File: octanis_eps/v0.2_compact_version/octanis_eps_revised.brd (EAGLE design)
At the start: 61.9 x 49.5 mm, 96 parts, among them IC1 OPA2333DGK, IC5 OPA2333DGK, IC7 OPA2333DGK, IC9 OPA2333DGK, Q1 FC-12M, Q2 N-HEXFET-2D_SOT232-, Q3 N-HEXFET-2D_SOT232-, Q4 N-HEXFET-2D_SOT232-

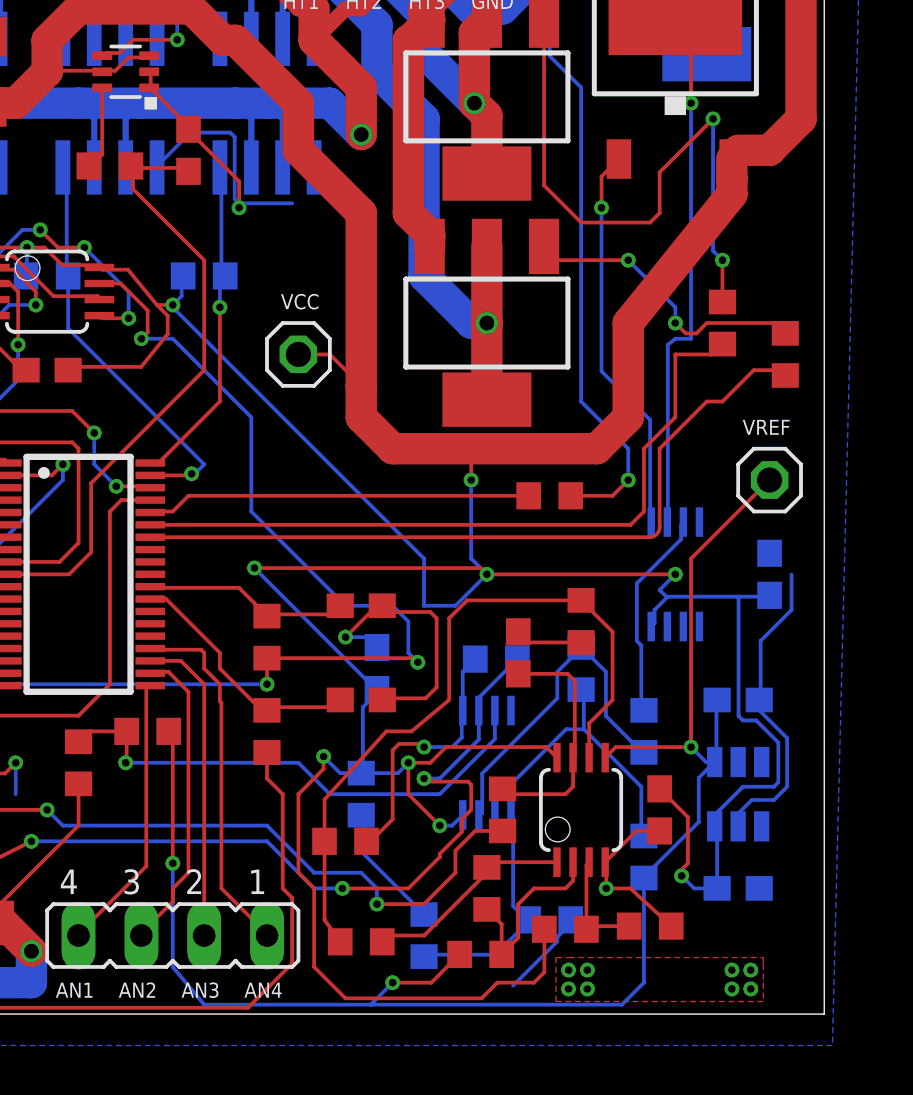
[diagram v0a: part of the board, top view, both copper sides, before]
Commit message: added pull down on heat EN entries
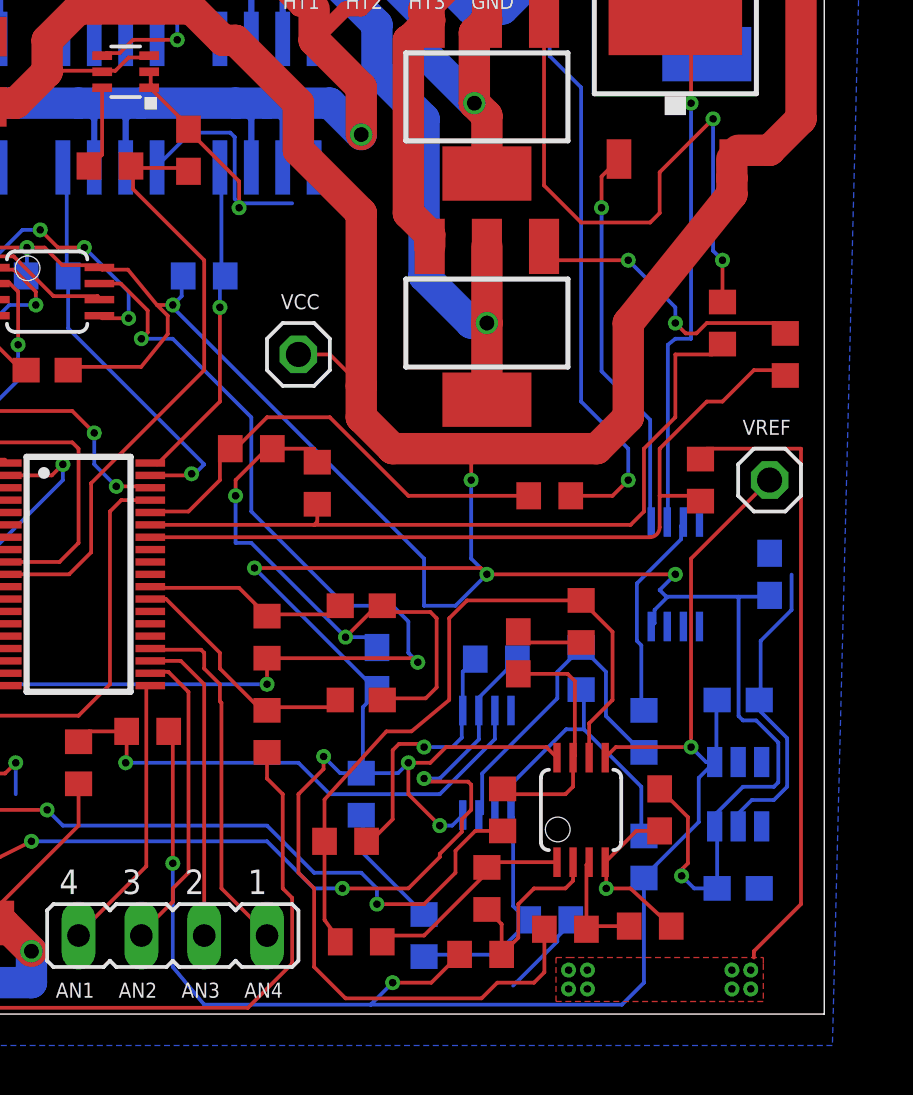
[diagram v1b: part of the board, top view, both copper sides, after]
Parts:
- added R42, R43, R44: 1M, rcl:R0603
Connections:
- net EN_HEAT1: now also R42.1
- net EN_HEAT2: now also R43.1
- net EN_HEAT3: now also R44.1
- net GND: now also R42.2, R43.2, R44.2
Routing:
- net GND: track 243.3 -> 282.0 mm, vias 28 -> 29
- net EN_HEAT3: track 15.6 -> 18.9 mm
- net EN_HEAT1: track 30.4 -> 32.1 mm
- net EN_HEAT2: track 29.1 -> 30.0 mm
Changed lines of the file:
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@@
 <attribute name="VALUE" x="39.37" y="53.975" size="1.27" layer="27"/>
+</element>
+<element name="R42" library="rcl" package="R0603" value="1M" x="56.896" y="52.07" smashed="yes" rot="R90">
+<attribute name="VALUE" x="57.785" y="50.419" size="1.27" layer="27" rot="R180"/>
+</element>
+<element name="R43" library="rcl" package="R0603" value="1M" x="41.402" y="51.943" smashed="yes" rot="R90">
+<attribute name="VALUE" x="43.307" y="50.8" size="1.27" layer="27" rot="R90"/>
+</element>
+<element name="R44" library="rcl" package="R0603" value="1M" x="38.735" y="53.34" smashed="yes">
+<attribute name="VALUE" x="37.592" y="53.975" size="1.27" layer="27"/>
 </element>
 </elements>
@@
 <wire x1="19.685" y1="53.34" x2="19.05" y2="53.34" width="0.1524" layer="16"/>
 <wire x1="19.05" y1="53.34" x2="18.8611" y2="53.5289" width="0.1524" layer="16"/>
+<contactref element="R43" pad="2"/>
+<contactref element="R44" pad="2"/>
+<contactref element="R42" pad="2"/>
+<wire x1="41.275" y1="53.34" x2="39.585" y2="53.34" width="0.1524" layer="1"/>
+<wire x1="41.275" y1="52.705" x2="41.275" y2="53.34" width="0.1524" layer="1"/>
+<wire x1="41.275" y1="52.705" x2="41.402" y2="52.793" width="0.1524" layer="1"/>
+<wire x1="60.96" y1="53.34" x2="57.15" y2="53.34" width="0.1524" layer="1"/>
+<wire x1="60.96" y1="34.925" x2="60.96" y2="53.34" width="0.1524" layer="1"/>
+<wire x1="59.055" y1="33.02" x2="60.96" y2="34.925" width="0.1524" layer="1"/>
+<wire x1="57.15" y1="53.34" x2="56.896" y2="52.92" width="0.1524" layer="1"/>
+<wire x1="59.055" y1="33.02" x2="59.055" y2="32.766" width="0.1524" layer="1"/>
+<wire x1="38.1" y1="52.07" x2="39.37" y2="53.34" width="0.1524" layer="1"/>
+<wire x1="38.1" y1="51.435" x2="38.1" y2="52.07" width="0.1524" layer="1"/>
+<wire x1="38.1" y1="49.53" x2="38.1" y2="51.435" width="0.1524" layer="16"/>
+<wire x1="38.735" y1="49.53" x2="38.1" y2="49.53" width="0.1524" layer="16"/>
+<wire x1="42.545" y1="45.72" x2="38.735" y2="49.53" width="0.1524" layer="16"/>
+<wire x1="39.37" y1="53.34" x2="39.585" y2="53.34" width="0.1524" layer="1"/>
+<via x="38.1" y="51.435" extent="1-16" drill="0.3048"/>
 </signal>
 <signal name="VCC">
@@
 <wire x1="35.3545" y1="57.9741" x2="35.3545" y2="58.717" width="0.1524" layer="1"/>
 <wire x1="35.3545" y1="58.717" x2="34.9218" y2="59.1497" width="0.1524" layer="1"/>
-<wire x1="58.42" y1="65.405" x2="58.16" y2="65.05" width="0" layer="19" extent="1-1"/>
+<wire x1="58.42" y1="65.405" x2="58.16" y2="65.05" width="0.1524" layer="1"/>
 </signal>
 <signal name="VREF">
@@
 <wire x1="34.65" y1="49.76" x2="54.84" y2="49.76" width="0.1524" layer="1"/>
 <wire x1="54.84" y1="49.76" x2="55.245" y2="50.165" width="0.1524" layer="1" curve="90"/>
-<wire x1="55.245" y1="50.165" x2="55.245" y2="53.34" width="0.1524" layer="1"/>
+<wire x1="55.245" y1="50.165" x2="55.245" y2="51.435" width="0.1524" layer="1"/>
+<wire x1="55.245" y1="51.435" x2="55.245" y2="53.34" width="0.1524" layer="1"/>
 <wire x1="55.245" y1="53.34" x2="57.15" y2="55.245" width="0.1524" layer="1"/>
 <wire x1="57.15" y1="55.245" x2="57.785" y2="55.245" width="0.1524" layer="1"/>
@@
 <wire x1="59.055" y1="56.515" x2="60.11" y2="56.515" width="0.1524" layer="1"/>
 <wire x1="60.11" y1="56.515" x2="60.325" y2="56.3" width="0.1524" layer="1"/>
+<contactref element="R42" pad="1"/>
+<wire x1="55.245" y1="51.435" x2="56.515" y2="51.435" width="0.1524" layer="1"/>
+<wire x1="56.515" y1="51.435" x2="56.896" y2="51.22" width="0.1524" layer="1"/>
 </signal>
 <signal name="EN_HEAT2">
 <contactref element="R2" pad="2"/>
 <contactref element="U$6" pad="33"/>
-<wire x1="34.65" y1="50.26" x2="54.07" y2="50.26" width="0.1524" layer="1"/>
+<wire x1="34.65" y1="50.26" x2="41.275" y2="50.26" width="0.1524" layer="1"/>
+<wire x1="41.275" y1="50.26" x2="54.07" y2="50.26" width="0.1524" layer="1"/>
 <wire x1="54.07" y1="50.26" x2="54.61" y2="50.8" width="0.1524" layer="1"/>
 <wire x1="54.61" y1="50.8" x2="54.61" y2="53.34" width="0.1524" layer="1"/>
@@
 <wire x1="55.88" y1="57.15" x2="57.365" y2="57.15" width="0.1524" layer="1"/>
 <wire x1="57.365" y1="57.15" x2="57.785" y2="57.57" width="0.1524" layer="1"/>
+<contactref element="R43" pad="1"/>
+<wire x1="41.402" y1="51.093" x2="41.402" y2="50.387" width="0.1524" layer="1"/>
+<wire x1="41.402" y1="50.387" x2="41.275" y2="50.26" width="0.1524" layer="1"/>
 </signal>
 <signal name="N$37">
@@
 <contactref element="R3" pad="2"/>
 <contactref element="U$6" pad="34"/>
-<wire x1="49.95" y1="51.435" x2="36.195" y2="51.435" width="0.1524" layer="1"/>
-<wire x1="36.195" y1="51.435" x2="35.56" y2="50.8" width="0.1524" layer="1"/>
-<wire x1="35.56" y1="50.8" x2="34.69" y2="50.8" width="0.1524" layer="1"/>
-<wire x1="34.69" y1="50.8" x2="34.65" y2="50.76" width="0.1524" layer="1"/>
+<contactref element="R44" pad="1"/>
+<wire x1="41.91" y1="54.61" x2="45.085" y2="51.435" width="0.1524" layer="1"/>
+<wire x1="45.085" y1="51.435" x2="49.95" y2="51.435" width="0.1524" layer="1"/>
+<wire x1="37.465" y1="52.07" x2="37.465" y2="53.34" width="0.1524" layer="1"/>
+<wire x1="36.195" y1="50.8" x2="37.465" y2="52.07" width="0.1524" layer="1"/>
+<wire x1="34.925" y1="50.8" x2="36.195" y2="50.8" width="0.1524" layer="1"/>
+<wire x1="37.465" y1="53.34" x2="37.885" y2="53.34" width="0.1524" layer="1"/>
+<wire x1="34.925" y1="50.8" x2="34.65" y2="50.76" width="0.1524" layer="1"/>
+<wire x1="39.37" y1="54.61" x2="38.1" y2="53.34" width="0.1524" layer="1"/>
+<wire x1="41.91" y1="54.61" x2="39.37" y2="54.61" width="0.1524" layer="1"/>
+<wire x1="38.1" y1="53.34" x2="37.885" y2="53.34" width="0.1524" layer="1"/>
 </signal>
 <signal name="DISSIP">

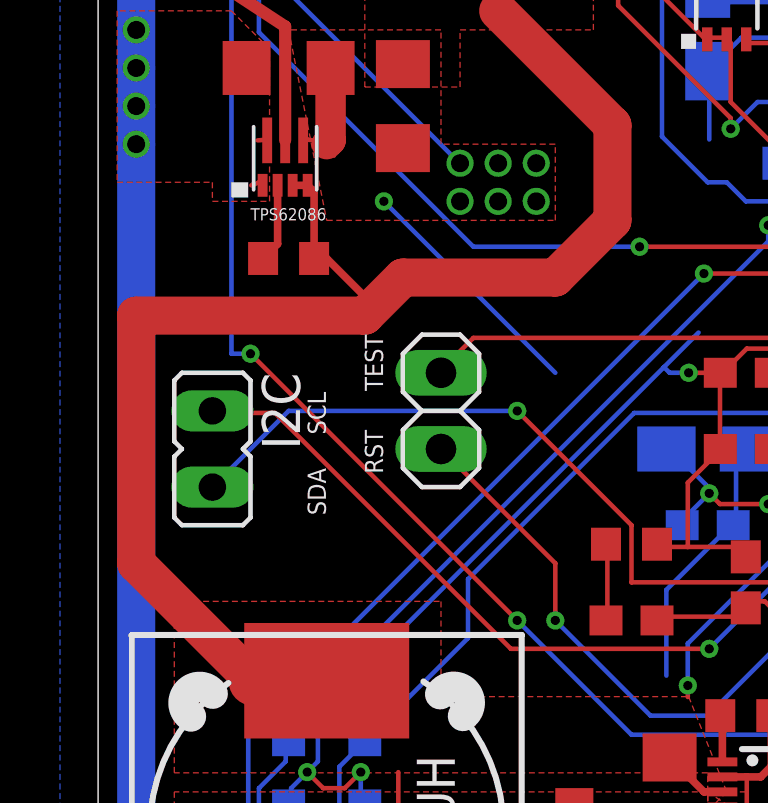
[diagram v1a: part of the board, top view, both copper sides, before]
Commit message: added 0Ohm jumper on discharge circuit
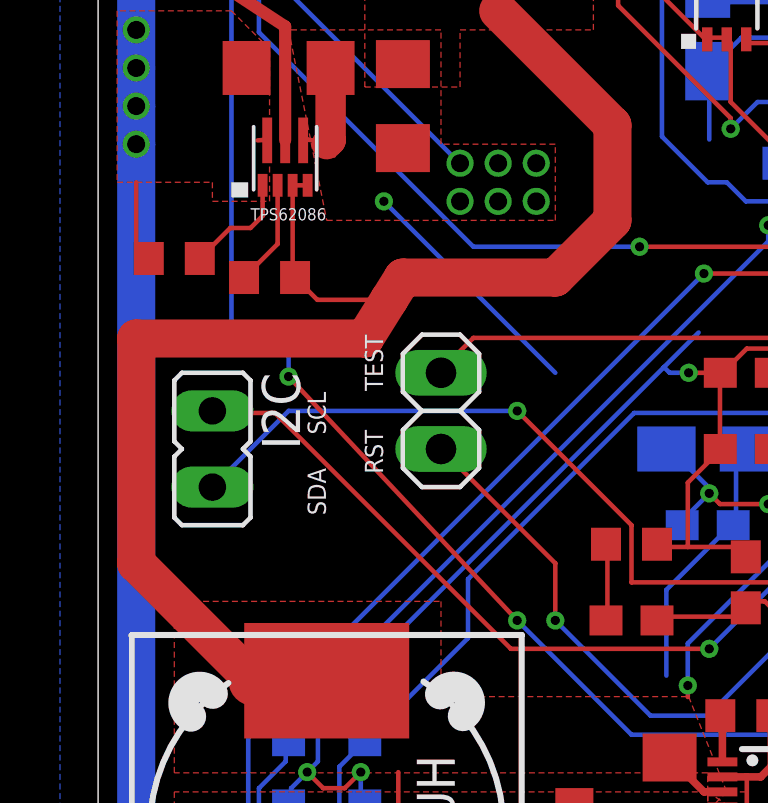
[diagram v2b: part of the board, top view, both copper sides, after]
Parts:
- added R45: 0Ohm, rcl:R0603
- moved R13 0.90 mm to (5.71, 56.5)
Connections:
- new net N$30: R45.2, U$5.1
- net BT+: now also R45.1; no longer U$5.1
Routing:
- net N$30: track 0.00 -> 3.70 mm
- net BT+: track 126.8 -> 129.1 mm
- net VCC: track 341.4 -> 342.4 mm
- net N$25: track 2.64 -> 3.54 mm
- net N$10: track 93.9 -> 94.5 mm
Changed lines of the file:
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@@
 <attribute name="VALUE" x="20.32" y="31.496" size="1.27" layer="27"/>
 </element>
-<element name="R13" library="rcl" package="R0603" value="1M" x="6.35" y="57.15" smashed="yes" rot="R180">
-<attribute name="VALUE" x="4.445" y="57.785" size="1.27" layer="27" rot="R180"/>
+<element name="R13" library="rcl" package="R0603" value="1M" x="5.715" y="56.515" smashed="yes" rot="R180">
+<attribute name="VALUE" x="7.62" y="57.785" size="1.27" layer="27" rot="R270"/>
 </element>
 <element name="C4" library="rcl" package="C1206" value="4.7u" x="19.05" y="39.116" smashed="yes" rot="R90">
@@
 <element name="R44" library="rcl" package="R0603" value="1M" x="38.735" y="53.34" smashed="yes">
 <attribute name="VALUE" x="37.592" y="53.975" size="1.27" layer="27"/>
+</element>
+<element name="R45" library="rcl" package="R0603" value="0Ohm" x="2.54" y="57.15" smashed="yes">
+<attribute name="VALUE" x="0" y="54.61" size="1.27" layer="27"/>
 </element>
 </elements>
@@
 <vertex x="16.51" y="79.375"/>
 </polygon>
-<wire x1="7.2" y1="57.15" x2="7.2" y2="59.3734" width="0.254" layer="1"/>
-<wire x1="7.2" y1="59.3734" x2="6.985" y2="59.5884" width="0.254" layer="1"/>
-<wire x1="6.48461875" y1="59.5884" x2="6.985" y2="59.5884" width="0.254" layer="1"/>
 <polygon width="0.254" layer="1">
 <vertex x="20.955" y="39.37"/>
@@
 <wire x1="7.62" y1="43.075" x2="5.185" y2="43.075" width="1.6764" layer="1"/>
 <wire x1="5.185" y1="43.075" x2="1.27" y2="46.99" width="1.27" layer="1"/>
-<wire x1="1.27" y1="46.99" x2="1.27" y2="55.245" width="1.27" layer="1"/>
-<wire x1="1.27" y1="55.245" x2="8.89" y2="55.245" width="1.27" layer="1"/>
-<wire x1="8.89" y1="55.245" x2="10.16" y2="56.515" width="1.27" layer="1"/>
+<wire x1="1.27" y1="46.99" x2="1.27" y2="54.483" width="1.27" layer="1"/>
+<wire x1="1.27" y1="54.483" x2="8.89" y2="54.483" width="1.27" layer="1"/>
+<wire x1="8.89" y1="54.483" x2="9.6962375" y2="55.772978125" width="1.27" layer="1"/>
+<wire x1="9.6962375" y1="55.772978125" x2="10.16" y2="56.515" width="1.27" layer="1"/>
 <wire x1="10.16" y1="56.515" x2="15.24" y2="56.515" width="1.27" layer="1"/>
 <wire x1="15.24" y1="56.515" x2="17.145" y2="58.42" width="1.27" layer="1"/>
 <wire x1="17.145" y1="58.42" x2="17.145" y2="61.595" width="1.27" layer="1"/>
 <wire x1="17.145" y1="61.595" x2="13.335" y2="65.405" width="1.27" layer="1"/>
-<wire x1="7.2" y1="57.15" x2="7.62" y2="57.15" width="0.254" layer="1"/>
-<wire x1="7.62" y1="57.15" x2="8.89" y2="55.88" width="0.254" layer="1"/>
-<wire x1="8.89" y1="55.88" x2="8.89" y2="55.245" width="0.254" layer="1"/>
 <contactref element="U$6" pad="16"/>
 <contactref element="C21" pad="2"/>
@@
 <wire x1="35.3545" y1="58.717" x2="34.9218" y2="59.1497" width="0.1524" layer="1"/>
 <wire x1="58.42" y1="65.405" x2="58.16" y2="65.05" width="0.1524" layer="1"/>
+<wire x1="6.565" y1="56.515" x2="6.48461875" y2="56.59538125" width="0.1524" layer="1"/>
+<wire x1="6.48461875" y1="56.59538125" x2="6.48461875" y2="59.5884" width="0.1524" layer="1"/>
+<wire x1="6.48461875" y1="59.5884" x2="6.985" y2="59.5884" width="0.1524" layer="1"/>
+<wire x1="6.565" y1="56.515" x2="7.307021875" y2="55.772978125" width="0.1524" layer="1"/>
+<wire x1="7.307021875" y1="55.772978125" x2="9.6962375" y2="55.772978125" width="0.1524" layer="1"/>
 </signal>
 <signal name="VREF">
@@
 <wire x1="4.445" y1="67.31" x2="5.08" y2="67.945" width="0.1524" layer="1"/>
 <wire x1="4.445" y1="53.975" x2="4.445" y2="67.31" width="0.1524" layer="16"/>
-<wire x1="5.08" y1="53.975" x2="4.445" y2="53.975" width="0.1524" layer="16"/>
-<wire x1="13.97" y1="45.085" x2="5.08" y2="53.975" width="0.1524" layer="1"/>
+<wire x1="6.35" y1="53.975" x2="4.445" y2="53.975" width="0.1524" layer="16"/>
 <wire x1="17.78" y1="41.275" x2="13.97" y2="45.085" width="0.1524" layer="16"/>
 <wire x1="23.495" y1="41.275" x2="17.78" y2="41.275" width="0.1524" layer="16"/>
@@
 <via x="5.715" y="71.755" extent="1-16" drill="0.3048"/>
 <via x="4.445" y="67.31" extent="1-16" drill="0.3048"/>
-<via x="5.08" y="53.975" extent="1-16" drill="0.3048"/>
-<via x="13.97" y="45.085" extent="1-16" drill="0.3048"/>
 <via x="39.37" y="43.815" extent="1-16" drill="0.3048"/>
 <wire x1="39.37" y1="44.87" x2="45.3" y2="44.87" width="0.1524" layer="1"/>
@@
 <wire x1="42.545" y1="46.99" x2="44.45" y2="46.99" width="0.1524" layer="16"/>
 <wire x1="44.45" y1="46.99" x2="45.085" y2="46.355" width="0.1524" layer="16"/>
+<via x="13.97" y="45.085" extent="1-16" drill="0.3048"/>
+<wire x1="13.97" y1="45.085" x2="6.35" y2="53.213" width="0.1524" layer="1"/>
+<via x="6.35" y="53.213" extent="1-16" drill="0.3048"/>
+<wire x1="6.35" y1="53.213" x2="6.35" y2="53.975" width="0.1524" layer="16"/>
 </signal>
 <signal name="N$15">
@@
 <contactref element="U$5" pad="7"/>
 <contactref element="C9" pad="2"/>
-<contactref element="U$5" pad="1"/>
 <contactref element="JP1" pad="1"/>
 <contactref element="JP1" pad="2"/>
@@
 <via x="1.27" y="63.5" extent="1-16" drill="0.6"/>
 <wire x1="19.05" y1="78.74" x2="1.27" y2="78.74" width="1.27" layer="16"/>
-<wire x1="5.361" y1="59.6858" x2="5.483859375" y2="59.5884" width="0.1524" layer="1"/>
-<wire x1="5.361" y1="59.6858" x2="5.106140625" y2="59.5884125" width="0.1524" layer="1"/>
 <wire x1="5.7184" y1="61.1154" x2="5.636259375" y2="61.087" width="0.1524" layer="1"/>
 <wire x1="5.7184" y1="61.1154" x2="5.3195" y2="61.0870125" width="0.1524" layer="1"/>
@@
 <wire x1="31.75" y1="38.1" x2="31.75" y2="39.79" width="0.1524" layer="1"/>
 <via x="1.27" y="64.77" extent="1-16" drill="0.6"/>
+<contactref element="R45" pad="1"/>
+<wire x1="1.69" y1="57.15" x2="1.27" y2="57.57" width="0.1524" layer="1"/>
+<wire x1="1.27" y1="57.57" x2="1.27" y2="59.69" width="0.1524" layer="1"/>
 </signal>
 <signal name="V_BT_MS">
@@
 <contactref element="U$5" pad="2"/>
 <contactref element="R13" pad="2"/>
-<wire x1="5.5" y1="57.15" x2="5.984240625" y2="57.634240625" width="0.254" layer="1"/>
-<wire x1="5.984240625" y1="57.634240625" x2="5.984240625" y2="59.5884" width="0.254" layer="1"/>
+<wire x1="4.865" y1="56.515" x2="5.984240625" y2="57.634240625" width="0.1524" layer="1"/>
+<wire x1="5.984240625" y1="57.634240625" x2="5.984240625" y2="59.5884" width="0.1524" layer="1"/>
 </signal>
 <signal name="N$29">
@@
 <wire x1="25.185" y1="33.846" x2="25.502" y2="34.163" width="0.1524" layer="1"/>
 </signal>
+<signal name="N$30">
+<contactref element="U$5" pad="1"/>
+<contactref element="R45" pad="2"/>
+<wire x1="3.39" y1="57.15" x2="4.406" y2="58.166" width="0.1524" layer="1"/>
+<wire x1="4.406" y1="58.166" x2="5.08" y2="58.166" width="0.1524" layer="1"/>
+<wire x1="5.08" y1="58.166" x2="5.483859375" y2="58.569859375" width="0.1524" layer="1"/>
+<wire x1="5.483859375" y1="58.569859375" x2="5.483859375" y2="59.5884" width="0.1524" layer="1"/>
+</signal>
 </signals>
